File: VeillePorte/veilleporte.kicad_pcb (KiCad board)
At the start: 2 copper layers, 45 parts, among them J10 P-MFC, J19 Conn_01x02_Socket, J20 ANTENNE 868MHz / 50 ohms, J21 UART2 / RUI3, J22 SWD, J23 CABLE MODULE VL53L4CD, J3 Conn_01x02_Pin, J4 Conn_01x02_Pin, SW1 RESET, U1 RAK3172(H) / EU868, U2 BQ25570

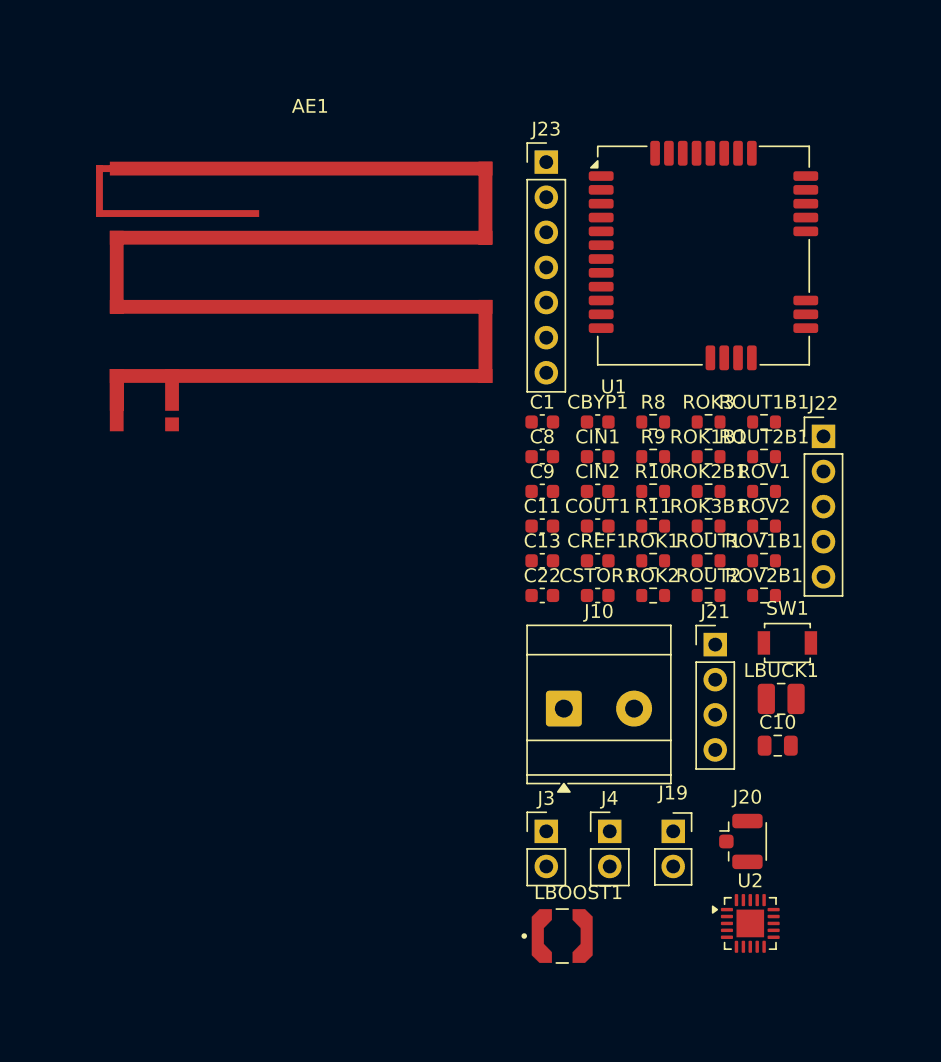
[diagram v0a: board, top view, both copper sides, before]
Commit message: Ajoute contour et cuivre quatre couches
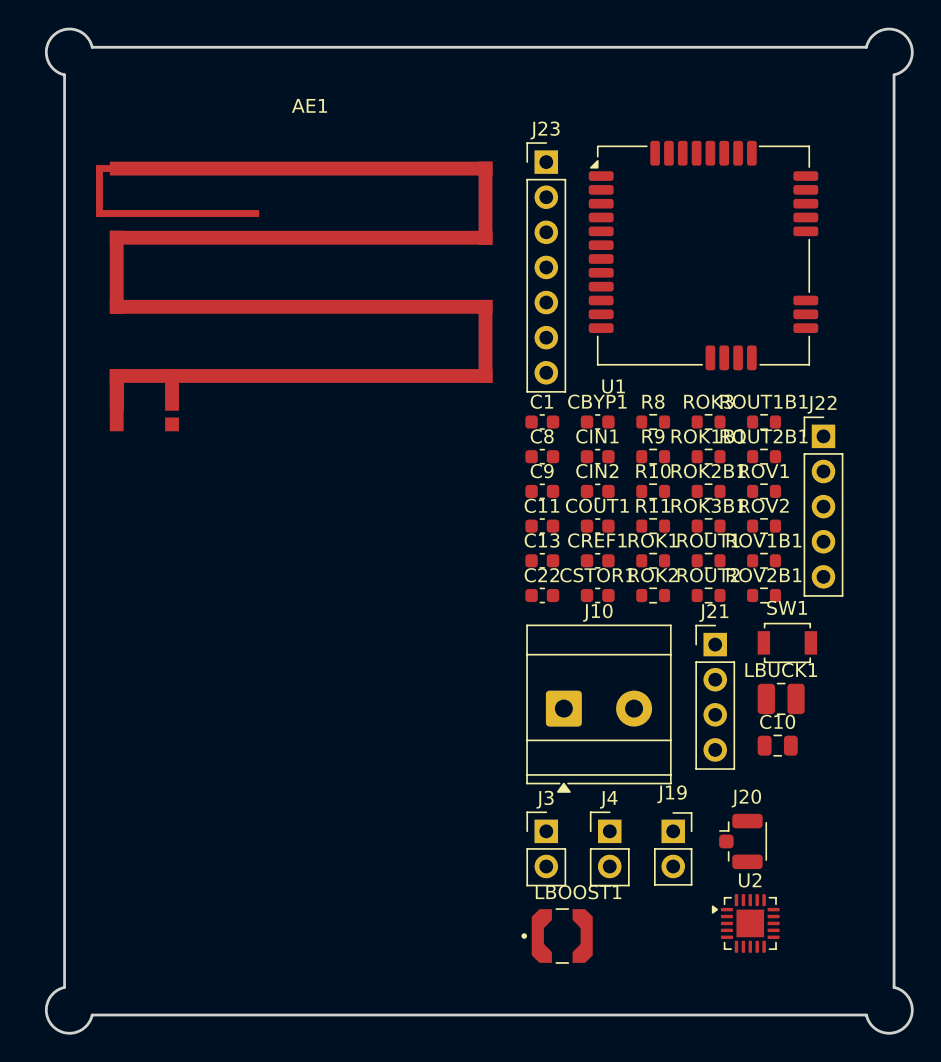
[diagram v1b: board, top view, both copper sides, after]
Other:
- board outline added: 62.6 x 72.6 mm
- copper layers 2 -> 4
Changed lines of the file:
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@@
 	(layers
 		(0 "F.Cu" signal)
+		(4 "In1.Cu" signal)
+		(6 "In2.Cu" signal)
 		(2 "B.Cu" signal)
 		(9 "F.Adhes" user "F.Adhesive")
@@
 	)
 	(embedded_fonts no)
+	(gr_line
+		(start 128.0000 28.0000)
+		(end 184.0000 28.0000)
+		(stroke (width 0.2) (type default))
+		(layer "Edge.Cuts")
+	)
+	(gr_arc
+		(start 184.0000 28.0000)
+		(mid 186.8284 27.1716)
+		(end 186.0000 30.0000)
+		(stroke (width 0.2) (type default))
+		(layer "Edge.Cuts")
+	)
+	(gr_line
+		(start 186.0000 30.0000)
+		(end 186.0000 96.0000)
+		(stroke (width 0.2) (type default))
+		(layer "Edge.Cuts")
+	)
+	(gr_arc
+		(start 186.0000 96.0000)
+		(mid 186.8284 98.8284)
+		(end 184.0000 98.0000)
+		(stroke (width 0.2) (type default))
+		(layer "Edge.Cuts")
+	)
+	(gr_line
+		(start 184.0000 98.0000)
+		(end 128.0000 98.0000)
+		(stroke (width 0.2) (type default))
+		(layer "Edge.Cuts")
+	)
+	(gr_arc
+		(start 128.0000 98.0000)
+		(mid 125.1716 98.8284)
+		(end 126.0000 96.0000)
+		(stroke (width 0.2) (type default))
+		(layer "Edge.Cuts")
+	)
+	(gr_line
+		(start 126.0000 96.0000)
+		(end 126.0000 30.0000)
+		(stroke (width 0.2) (type default))
+		(layer "Edge.Cuts")
+	)
+	(gr_arc
+		(start 126.0000 30.0000)
+		(mid 125.1716 27.1716)
+		(end 128.0000 28.0000)
+		(stroke (width 0.2) (type default))
+		(layer "Edge.Cuts")
+	)
 )

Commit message: Place le RAK au centre et les connecteurs au pourtour
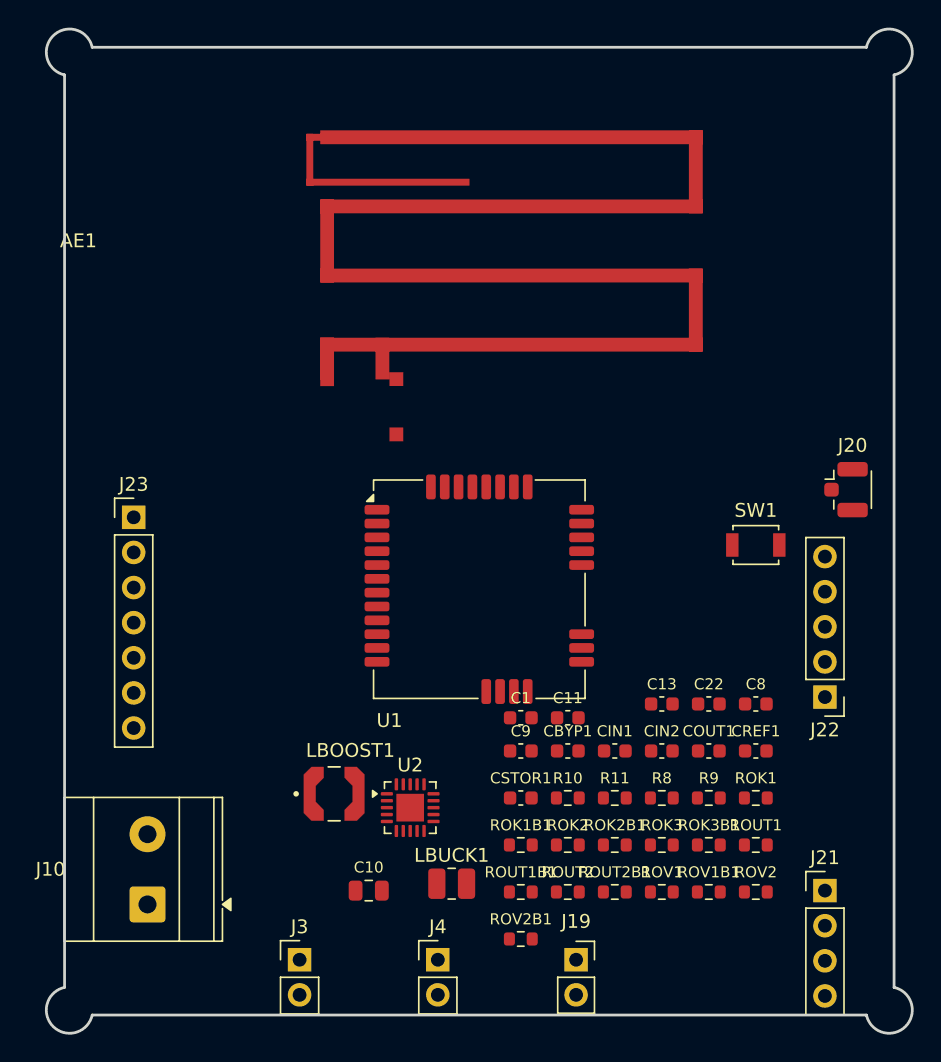
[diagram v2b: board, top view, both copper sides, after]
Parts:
- moved J23 39.4 mm to (131.0, 62.0)
- moved ROUT1B1 38.3 mm to (159.0, 89.1)
- moved ROUT2B1 33.3 mm to (165.8, 89.1)
- moved J10 33.3 mm to (132.0, 90.0), turned to 90 degrees
- moved C10 31.4 mm to (148.0, 89.0)
- moved ROK1B1 31.2 mm to (159.0, 85.7)
- moved ROK3 30.8 mm to (169.2, 85.7)
- moved ROV2B1 30.4 mm to (159.0, 92.5)
- moved ROV1 29.9 mm to (169.2, 89.1)
- moved U1 29.1 mm to (156.0, 67.2)
- moved LBUCK1 27.3 mm to (154.0, 88.5)
- moved R8 27.2 mm to (169.2, 82.3)
- moved J20 26.6 mm to (183.0, 60.0)
- moved ROV2 26.5 mm to (176.0, 89.1)
- moved ROK2B1 26.5 mm to (165.8, 85.7)
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
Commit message: Ajoute adaptation RF 868 MHz avec shunts DNP
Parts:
- removed J20: ANTENNE 868MHz / 50 ohms, Connector_Coaxial:U.FL_Hirose_U.FL-R-SMT-1_Vertical
- added C6: DNP, C_0603_1608Metric, F.Cu at (143.0, 69.5)
- added L1: DNP, L_0603_1608Metric, F.Cu at (168.0, 56.0)
- added R12: 0R, R_0603_1608Metric, F.Cu at (143.5, 63.0)
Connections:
- net 'EN renamed GND
- AE1 pad 1: /RF -> /RF_ANT
- U1 pad 12: /RF -> /RF_SRC
